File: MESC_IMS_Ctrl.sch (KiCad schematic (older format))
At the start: 69 parts, among them J1 Conn_01x08_Female, J10 Conn_01x04_Male, J2 Conn_01x08_Female, J3 Conn_01x08_Female, J4 Conn_01x06_Male, J5 Conn_ARM_JTAG_SWD_10, J6 USB_C_Receptacle_USB2.0, J7 Conn_01x03_Male, J8 Conn_01x04_Male, J9 Conn_01x08_Male, U1 STM32F303CBTx, Y1 ASE-8.000MHZ-LC-T

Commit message: Removed coupled inductor
Added TPS61041DB
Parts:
- J4: LCSC (none) -> C225237
- J9: LCSC (none) -> C225239
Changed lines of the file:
@@
 F 2 "Connector_JST:JST_PH_S6B-PH-SM4-TB_1x06-1MP_P2.00mm_Horizontal" H 650 3850 50  0001 C CNN
 F 3 "~" H 650 3850 50  0001 C CNN
-F 4 "~" H 650 3850 50  0001 C CNN "LCSC"
+F 4 "C225237	" H 650 3850 50  0001 C CNN "LCSC"
 	1    650  3850
 	1    0    0    1
@@
 F 2 "Connector_JST:JST_PH_S8B-PH-SM4-TB_1x08-1MP_P2.00mm_Horizontal" H 2950 6700 50  0001 C CNN
 F 3 "~" H 2950 6700 50  0001 C CNN
-F 4 "~" H 2950 6700 50  0001 C CNN "LCSC"
+F 4 "C225239" H 2950 6700 50  0001 C CNN "LCSC"
 	1    2950 6700
 	1    0    0    -1

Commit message: Tweaking potential dividers
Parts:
- R24, R25: footprint Resistor_SMD:R_0402_1005Metric -> Resistor_SMD:R_0603_1608Metric
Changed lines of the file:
@@
 F 0 "R24" H 6220 6196 50  0000 L CNN
 F 1 "82k" H 6220 6105 50  0000 L CNN
-F 2 "Resistor_SMD:R_0402_1005Metric" V 6080 6150 50  0001 C CNN
+F 2 "Resistor_SMD:R_0603_1608Metric" V 6080 6150 50  0001 C CNN
 F 3 "~" H 6150 6150 50  0001 C CNN
 F 4 "C4142" H 6150 6150 50  0001 C CNN "LCSC"
@@
 F 0 "R25" H 6220 6696 50  0000 L CNN
 F 1 "1k5" H 6220 6605 50  0000 L CNN
-F 2 "Resistor_SMD:R_0402_1005Metric" V 6080 6650 50  0001 C CNN
+F 2 "Resistor_SMD:R_0603_1608Metric" V 6080 6650 50  0001 C CNN
 F 3 "~" H 6150 6650 50  0001 C CNN
 F 4 "C25867" H 6150 6650 50  0001 C CNN "LCSC"

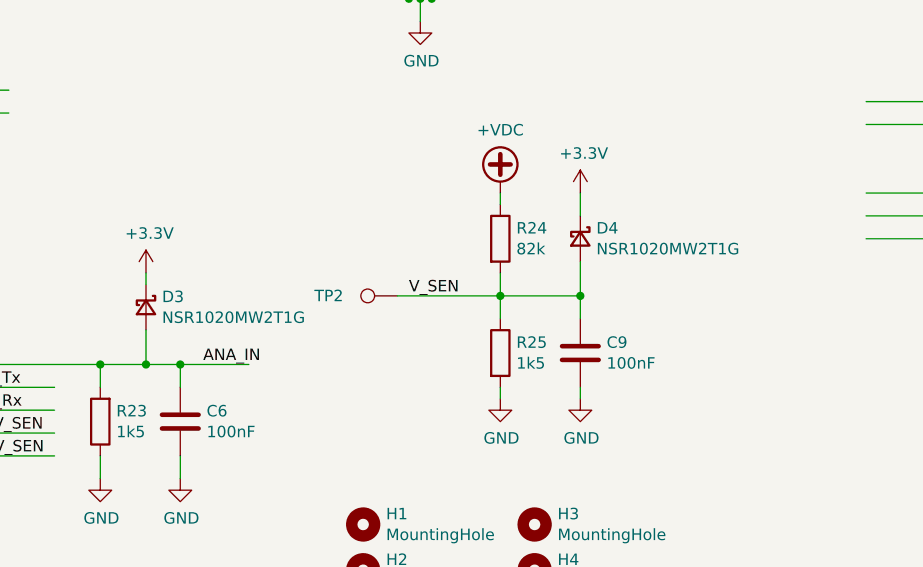
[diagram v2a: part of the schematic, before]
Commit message: Routing nearly complete
some diodes made smaller
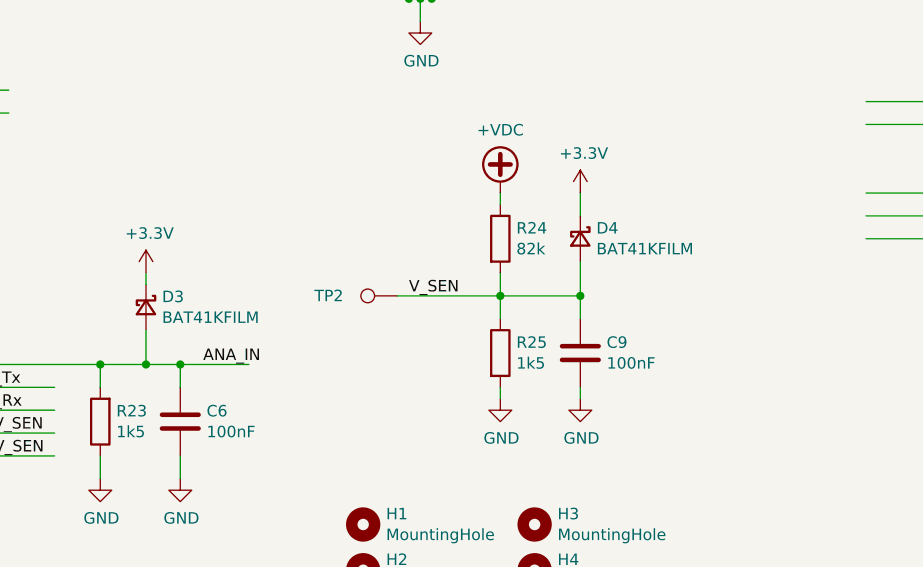
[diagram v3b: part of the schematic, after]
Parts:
- D3, D4: value NSR1020MW2T1G -> BAT41KFILM; footprint Diode_SMD:D_SOD-323 -> Diode_SMD:D_SOD-523
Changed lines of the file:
@@
 	1000 6050 1000 5950
-$Comp
-L Device:D_Schottky_Small D1
-U 1 1 6076F431
-P 1000 5850
-F 0 "D1" V 1046 5780 50  0000 R CNN
-F 1 "NSR1020MW2T1G" V 955 5780 50  0000 R CNN
-F 2 "Diode_SMD:D_SOD-323" V 1000 5850 50  0001 C CNN
-F 3 "~" V 1000 5850 50  0001 C CNN
-	1    1000 5850
-	0    -1   -1   0
-$EndComp
 $Comp
 L power:+3V3 #PWR0103
@@
 AR Path="/60813B50" Ref="D4"  Part="1"
 F 0 "D4" V 6454 6220 50  0000 L CNN
-F 1 "NSR1020MW2T1G" V 6545 6220 50  0000 L CNN
-F 2 "Diode_SMD:D_SOD-323" V 6500 6150 50  0001 C CNN
+F 1 "BAT41KFILM" V 6545 6220 50  0000 L CNN
+F 2 "Diode_SMD:D_SOD-523" V 6500 6150 50  0001 C CNN
 F 3 "~" V 6500 6150 50  0001 C CNN
 	1    6500 6150
@@
 ANA_IN
 $Comp
-L Device:D_Schottky_Small D?
-U 1 1 60F31067
-P 4600 6450
-AR Path="/6070CE7F/60F31067" Ref="D?"  Part="1"
-AR Path="/6074FE4E/60F31067" Ref="D?"  Part="1"
-AR Path="/6075047A/60F31067" Ref="D?"  Part="1"
-AR Path="/60F31067" Ref="D3"  Part="1"
-F 0 "D3" V 4554 6520 50  0000 L CNN
-F 1 "NSR1020MW2T1G" V 4645 6520 50  0000 L CNN
-F 2 "Diode_SMD:D_SOD-323" V 4600 6450 50  0001 C CNN
-F 3 "~" V 4600 6450 50  0001 C CNN
-F 4 "" V 4600 6450 50  0001 C CNN "LCSC"
-	1    4600 6450
-	0    1    1    0
-$EndComp
-$Comp
 L power:+3.3V #PWR?
 U 1 1 60F3106D
@@
 Text Label 4700 2650 0    50   ~ 0
 CLK
+$Comp
+L Device:D_Schottky_Small D1
+U 1 1 6076F431
+P 1000 5850
+F 0 "D1" V 1046 5780 50  0000 R CNN
+F 1 "NSR1020MW2T1G" V 955 5780 50  0000 R CNN
+F 2 "Diode_SMD:D_SOD-323" V 1000 5850 50  0001 C CNN
+F 3 "~" V 1000 5850 50  0001 C CNN
+	1    1000 5850
+	0    -1   -1   0
+$EndComp
+$Comp
+L Device:D_Schottky_Small D?
+U 1 1 60F31067
+P 4600 6450
+AR Path="/6070CE7F/60F31067" Ref="D?"  Part="1"
+AR Path="/6074FE4E/60F31067" Ref="D?"  Part="1"
+AR Path="/6075047A/60F31067" Ref="D?"  Part="1"
+AR Path="/60F31067" Ref="D3"  Part="1"
+F 0 "D3" V 4554 6520 50  0000 L CNN
+F 1 "BAT41KFILM" V 4645 6520 50  0000 L CNN
+F 2 "Diode_SMD:D_SOD-523" V 4600 6450 50  0001 C CNN
+F 3 "~" V 4600 6450 50  0001 C CNN
+F 4 "" V 4600 6450 50  0001 C CNN "LCSC"
+	1    4600 6450
+	0    1    1    0
+$EndComp
 $EndSCHEMATC

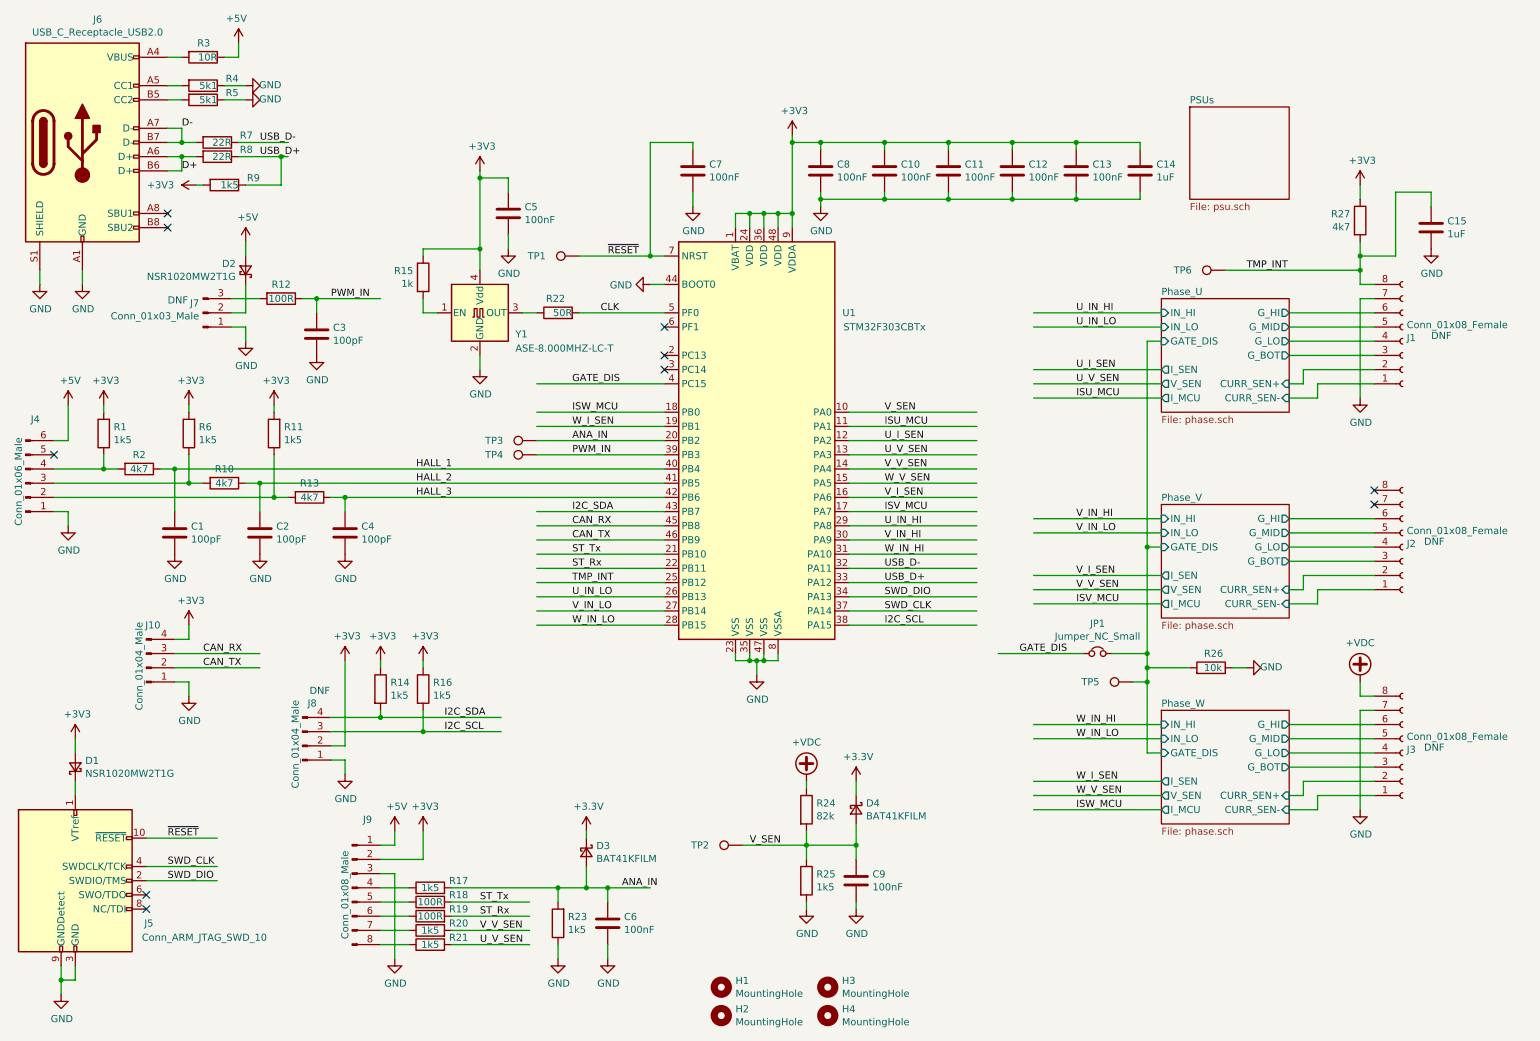
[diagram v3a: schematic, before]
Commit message: Updated part numbers
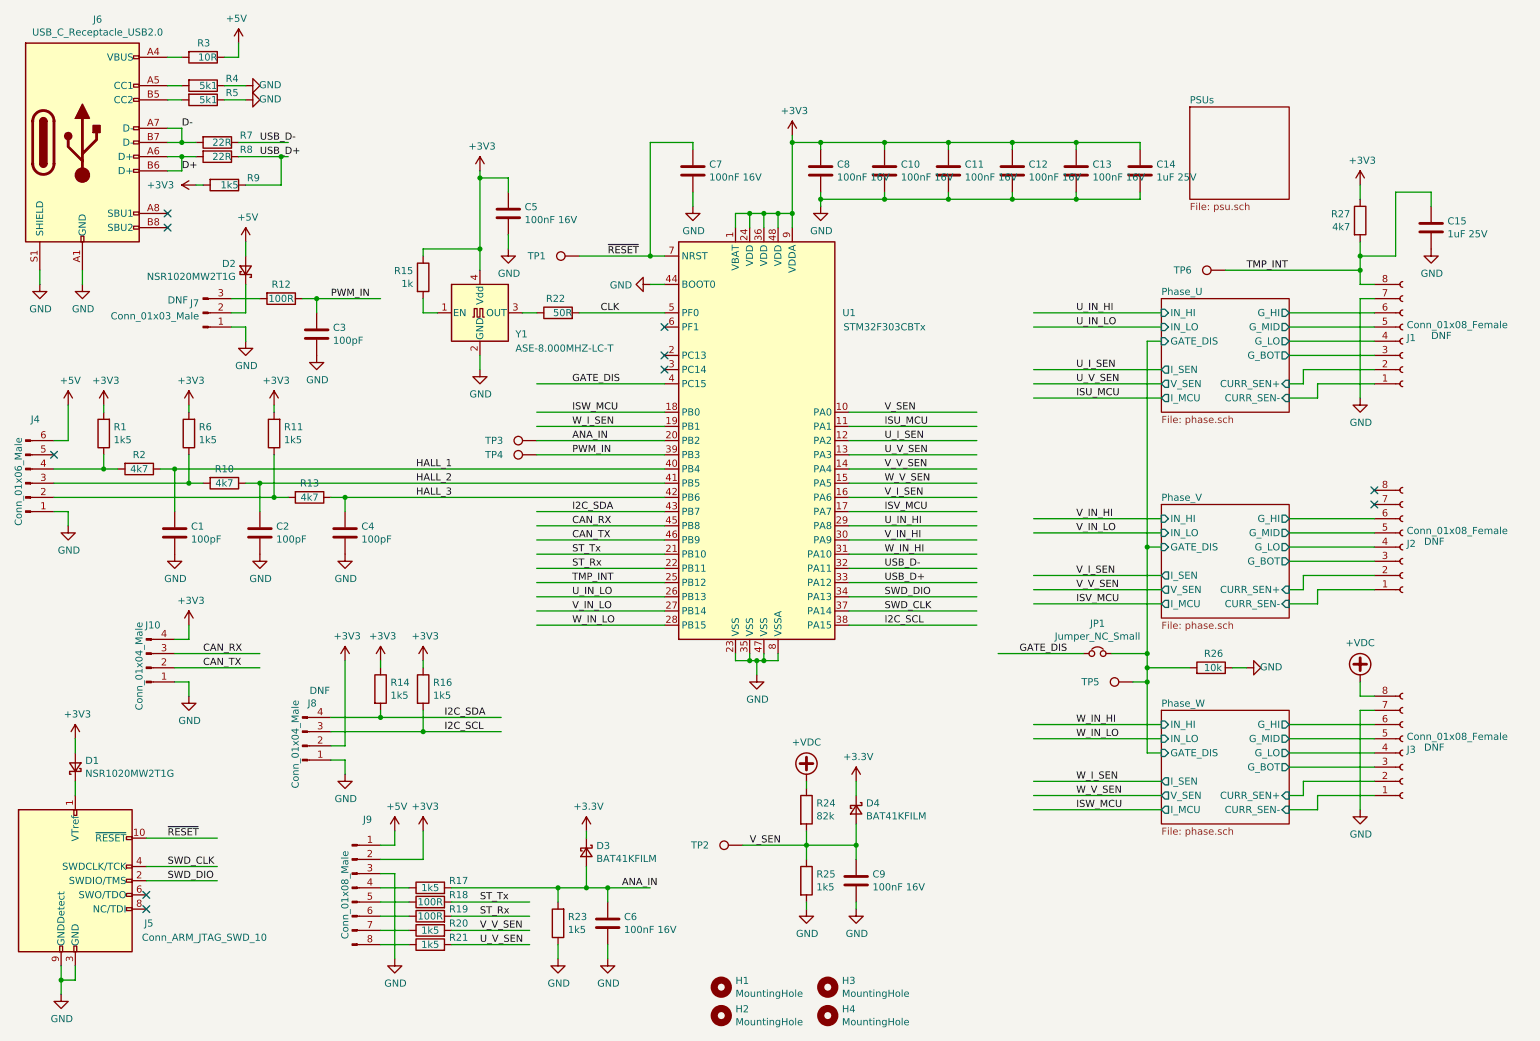
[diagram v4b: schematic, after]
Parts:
- C1, C2, C3, C4, H1, H2, H3, H4, J1, J10, J2, J3, J4, J7, J8, J9, JP1, R1, R10, R11, R12, R13, R14, R15, R16, R17, R18, R19, R2, R20, R21, R22, R23, R26, R27, R3, R4, R5, R6, R7, R8, R9, TP1, TP2, TP3, TP4, TP5, TP6: Checked (none) -> Yes
- C10, C11, C12, C13, C5, C6, C7, C8, C9: value 100nF -> 100nF 16V; Checked (none) -> Yes
- C14, C15: value 1uF -> 1uF 25V; Checked (none) -> Yes
- D1, D2: Checked (none) -> Yes; LCSC (none) -> C116953
- D3, D4: Checked (none) -> Yes; LCSC (none) -> C73150
- J5: Checked (none) -> Yes; LCSC C165948 -> C239059
- J6: Checked (none) -> Yes; LCSC (none) -> C165948
- R24: Checked (none) -> Yes; LCSC C4142 -> C23254
- R25: Checked (none) -> Yes; LCSC C25867 -> C22843
- U1: Checked (none) -> Yes - backorder
- Y1: Checked (none) -> Yes; LCSC C39097 -> C295522

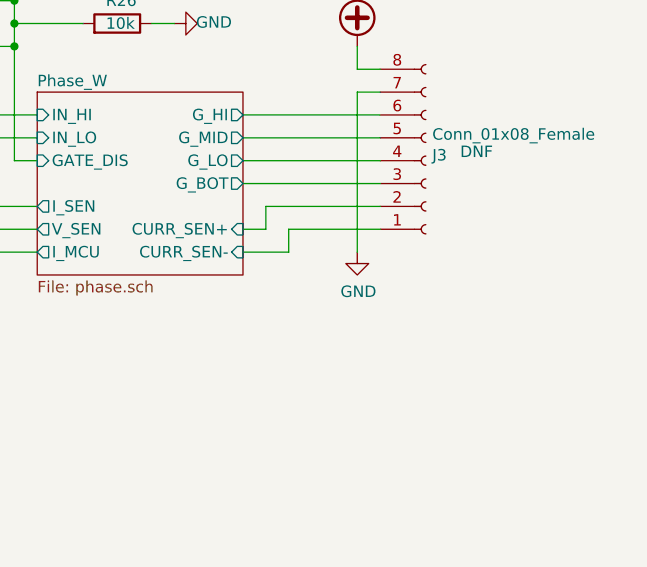
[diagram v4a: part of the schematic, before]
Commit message: Adding 0V TP and labels
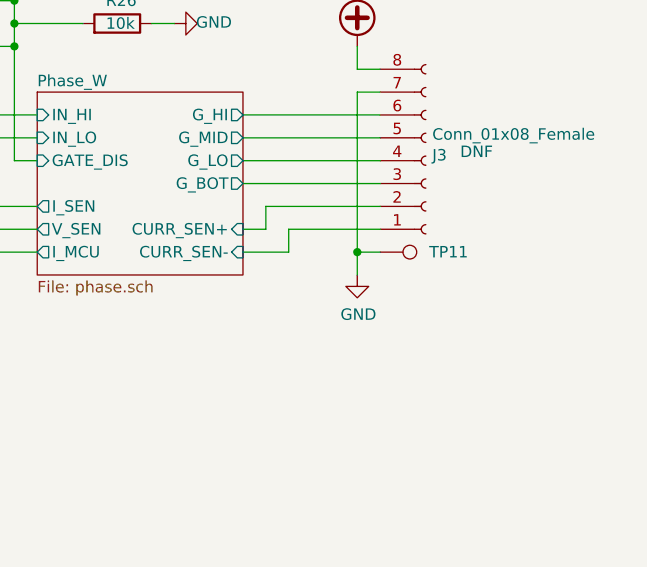
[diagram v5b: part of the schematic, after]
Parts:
- added TP11: TestPoint, TestPoint:TestPoint_Pad_D1.5mm, symbol Connector:TestPoint
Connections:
- wire segments 287 -> 289
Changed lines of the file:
@@
 L power:GND #PWR031
 U 1 1 6072B0D2
-P 10050 6150
-F 0 "#PWR031" H 10050 5900 50  0001 C CNN
-F 1 "GND" H 10055 5977 50  0000 C CNN
-F 2 "" H 10050 6150 50  0001 C CNN
-F 3 "" H 10050 6150 50  0001 C CNN
-	1    10050 6150
+P 10050 6250
+F 0 "#PWR031" H 10050 6000 50  0001 C CNN
+F 1 "GND" H 10055 6077 50  0000 C CNN
+F 2 "" H 10050 6250 50  0001 C CNN
+F 3 "" H 10050 6250 50  0001 C CNN
+	1    10050 6250
 	1    0    0    -1
 $EndComp
@@
 	0    1    1    0
 $EndComp
+$Comp
+L Connector:TestPoint TP11
+U 1 1 609AA071
+P 10150 6150
+F 0 "TP11" V 10150 6450 50  0000 C CNN
+F 1 "TestPoint" V 10254 6222 50  0001 C CNN
+F 2 "TestPoint:TestPoint_Pad_D1.5mm" H 10350 6150 50  0001 C CNN
+F 3 "~" H 10350 6150 50  0001 C CNN
+F 4 "~" H 10150 6150 50  0001 C CNN "LCSC"
+F 5 "Yes" H 10150 6150 50  0001 C CNN "Checked"
+	1    10150 6150
+	0    1    -1   0
+$EndComp
+Wire Wire Line
+	10150 6150 10050 6150
+Connection ~ 10050 6150
+Wire Wire Line
+	10050 6150 10050 6250
 $EndSCHEMATC
